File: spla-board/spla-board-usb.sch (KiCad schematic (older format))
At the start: 27 parts, among them J1 USB_B_Micro, U2 FT2232H, U3 93LC66B, X1 FT5HNBPK12.0-T1

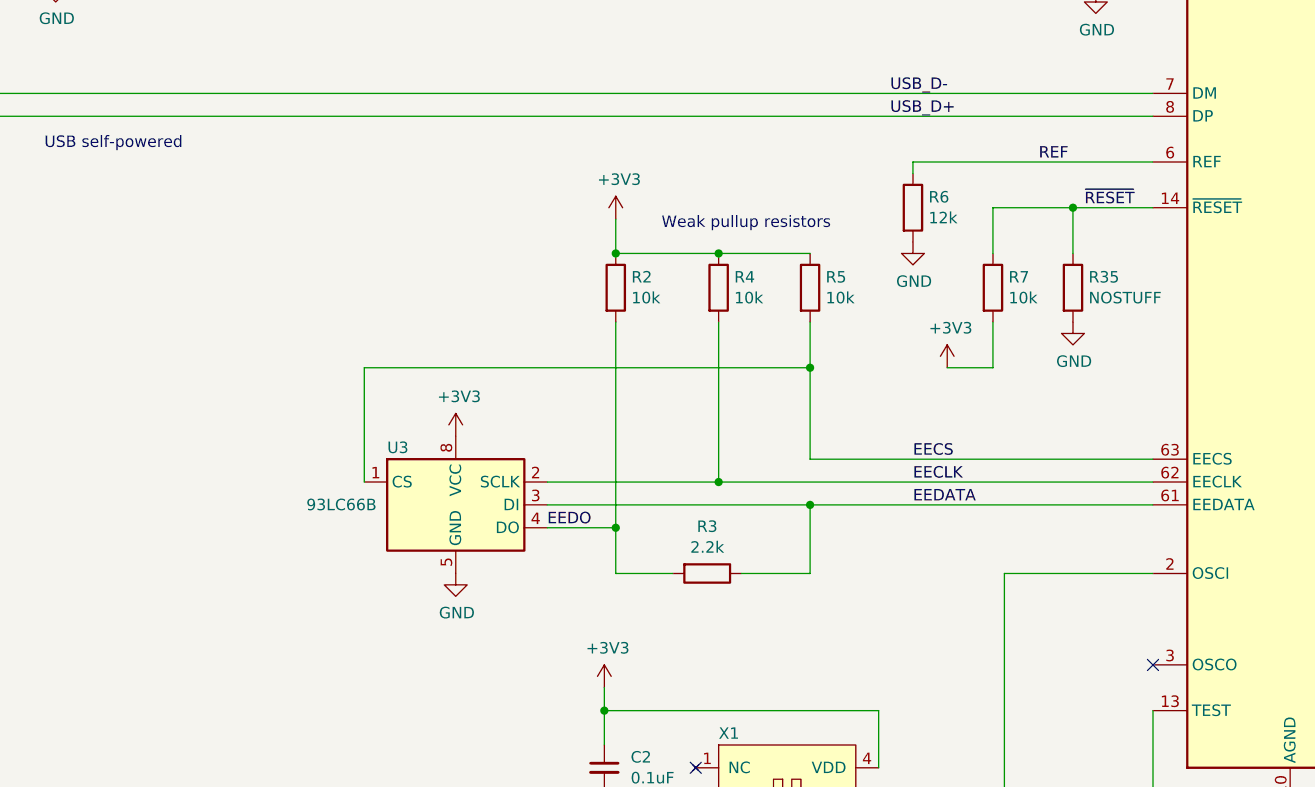
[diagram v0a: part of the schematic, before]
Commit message: schematic: Swap FTDI REF resistor from 5% (oops) to 1%.
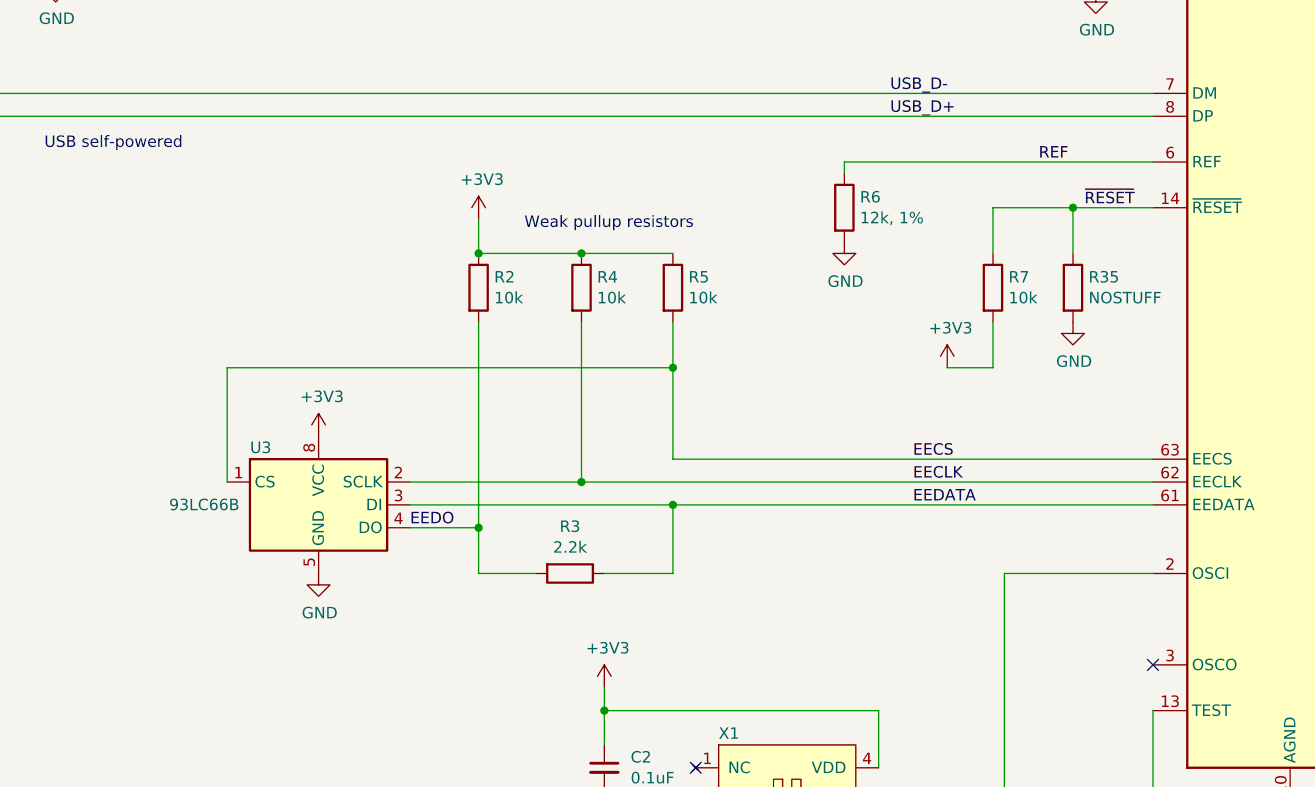
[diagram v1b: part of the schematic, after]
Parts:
- R6: value 12k -> 12k, 1%; Digikey RMCF0603JT12K0CT-ND -> RMCF0603FT12K0CT-ND; Manufacturer Id RMCF0603JT12K0 -> RMCF0603FT12K0
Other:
- moved on the sheet: R2, R3, R4, R5, R6, U3
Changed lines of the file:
@@
 L power:GND #PWR0104
 U 1 1 5E558255
-P 5700 6850
-F 0 "#PWR0104" H 5700 6600 50  0001 C CNN
-F 1 "GND" H 5705 6677 50  0000 C CNN
-F 2 "" H 5700 6850 50  0001 C CNN
-F 3 "" H 5700 6850 50  0001 C CNN
-	1    5700 6850
-	1    0    0    -1
-$EndComp
-Wire Wire Line
-	7250 6350 8750 6350
-Wire Wire Line
-	5300 5950 7250 5950
-Wire Wire Line
-	5300 5950 5300 6450
-Wire Wire Line
-	7250 5950 7250 6350
+P 5100 6850
+F 0 "#PWR0104" H 5100 6600 50  0001 C CNN
+F 1 "GND" H 5105 6677 50  0000 C CNN
+F 2 "" H 5100 6850 50  0001 C CNN
+F 3 "" H 5100 6850 50  0001 C CNN
+	1    5100 6850
+	1    0    0    -1
+$EndComp
+Wire Wire Line
+	6650 6350 8750 6350
+Wire Wire Line
+	4700 5950 6650 5950
+Wire Wire Line
+	4700 5950 4700 6450
+Wire Wire Line
+	6650 5950 6650 6350
 $Comp
 L Device:R R3
 U 1 1 5E55BD51
-P 6800 6850
-F 0 "R3" V 6595 6850 50  0000 C CNN
-F 1 "2.2k" V 6686 6850 50  0000 C CNN
-F 2 "Resistor_SMD:R_0603_1608Metric" V 6840 6840 50  0001 C CNN
-F 3 "~" H 6800 6850 50  0001 C CNN
-F 4 "RMCF0603JT2K20CT-ND" H 6800 6850 50  0001 C CNN "Digikey"
-F 5 "Stackpole Electronics Inc" H 6800 6850 50  0001 C CNN "Manufacturer"
-F 6 "RMCF0603JT2K20" H 6800 6850 50  0001 C CNN "Manufacturer Id"
-	1    6800 6850
+P 6200 6850
+F 0 "R3" V 5995 6850 50  0000 C CNN
+F 1 "2.2k" V 6086 6850 50  0000 C CNN
+F 2 "Resistor_SMD:R_0603_1608Metric" V 6240 6840 50  0001 C CNN
+F 3 "~" H 6200 6850 50  0001 C CNN
+F 4 "RMCF0603JT2K20CT-ND" H 6200 6850 50  0001 C CNN "Digikey"
+F 5 "Stackpole Electronics Inc" H 6200 6850 50  0001 C CNN "Manufacturer"
+F 6 "RMCF0603JT2K20" H 6200 6850 50  0001 C CNN "Manufacturer Id"
+	1    6200 6850
 	0    1    1    0
 $EndComp
 Wire Wire Line
-	6100 6650 6400 6650
-Wire Wire Line
-	6400 6650 6400 6850
-Wire Wire Line
-	6400 6850 6650 6850
-Wire Wire Line
-	6100 6550 7250 6550
-Wire Wire Line
-	6950 6850 7250 6850
-Wire Wire Line
-	6100 6450 6850 6450
-Wire Wire Line
-	7250 6550 7250 6850
-Wire Wire Line
-	8750 6550 7250 6550
-Connection ~ 7250 6550
-Wire Wire Line
-	7250 5450 6850 5450
-Connection ~ 6850 5450
-Wire Wire Line
-	6850 5450 6400 5450
-Wire Wire Line
-	6400 5450 6400 5300
-Connection ~ 6400 5450
-Wire Wire Line
-	6400 5750 6400 6650
-Connection ~ 6400 6650
-Wire Wire Line
-	6850 5750 6850 6450
-Connection ~ 6850 6450
-Wire Wire Line
-	6850 6450 8750 6450
-Wire Wire Line
-	7250 5750 7250 5950
-Connection ~ 7250 5950
+	5500 6650 5800 6650
+Wire Wire Line
+	5800 6650 5800 6850
+Wire Wire Line
+	5800 6850 6050 6850
+Wire Wire Line
+	5500 6550 6650 6550
+Wire Wire Line
+	6350 6850 6650 6850
+Wire Wire Line
+	5500 6450 6250 6450
+Wire Wire Line
+	6650 6550 6650 6850
+Wire Wire Line
+	8750 6550 6650 6550
+Connection ~ 6650 6550
+Wire Wire Line
+	6650 5450 6250 5450
+Connection ~ 6250 5450
+Wire Wire Line
+	6250 5450 5800 5450
+Wire Wire Line
+	5800 5450 5800 5300
+Connection ~ 5800 5450
+Wire Wire Line
+	5800 5750 5800 6650
+Connection ~ 5800 6650
+Wire Wire Line
+	6250 5750 6250 6450
+Connection ~ 6250 6450
+Wire Wire Line
+	6250 6450 8750 6450
+Wire Wire Line
+	6650 5750 6650 5950
+Connection ~ 6650 5950
 $Comp
 L power:GND #PWR0105
@@
 	8750 7850 8900 7850
 Connection ~ 8900 7850
-Text Notes 6600 5350 0    50   ~ 0
+Text Notes 6000 5350 0    50   ~ 0
 Weak pullup resistors
 Wire Wire Line
@@
 L power:GND #PWR0108
 U 1 1 5E616CF7
-P 7700 5400
-F 0 "#PWR0108" H 7700 5150 50  0001 C CNN
-F 1 "GND" H 7705 5227 50  0000 C CNN
-F 2 "" H 7700 5400 50  0001 C CNN
-F 3 "" H 7700 5400 50  0001 C CNN
-	1    7700 5400
-	1    0    0    -1
-$EndComp
-Wire Wire Line
-	7700 5050 7700 5100
+P 7400 5400
+F 0 "#PWR0108" H 7400 5150 50  0001 C CNN
+F 1 "GND" H 7405 5227 50  0000 C CNN
+F 2 "" H 7400 5400 50  0001 C CNN
+F 3 "" H 7400 5400 50  0001 C CNN
+	1    7400 5400
+	1    0    0    -1
+$EndComp
+Wire Wire Line
+	7400 5050 7400 5100
 Wire Wire Line
 	8050 5950 8050 5750
@@
 L power:+3V3 #PWR0110
 U 1 1 5E64A1B5
-P 5700 6250
-F 0 "#PWR0110" H 5700 6100 50  0001 C CNN
-F 1 "+3V3" H 5715 6423 50  0000 C CNN
-F 2 "" H 5700 6250 50  0001 C CNN
-F 3 "" H 5700 6250 50  0001 C CNN
-	1    5700 6250
+P 5100 6250
+F 0 "#PWR0110" H 5100 6100 50  0001 C CNN
+F 1 "+3V3" H 5115 6423 50  0000 C CNN
+F 2 "" H 5100 6250 50  0001 C CNN
+F 3 "" H 5100 6250 50  0001 C CNN
+	1    5100 6250
 	1    0    0    -1
 $EndComp
@@
 L power:+3V3 #PWR0112
 U 1 1 5E64B6A0
-P 6400 5300
-F 0 "#PWR0112" H 6400 5150 50  0001 C CNN
-F 1 "+3V3" H 6415 5473 50  0000 C CNN
-F 2 "" H 6400 5300 50  0001 C CNN
-F 3 "" H 6400 5300 50  0001 C CNN
-	1    6400 5300
+P 5800 5300
+F 0 "#PWR0112" H 5800 5150 50  0001 C CNN
+F 1 "+3V3" H 5815 5473 50  0000 C CNN
+F 2 "" H 5800 5300 50  0001 C CNN
+F 3 "" H 5800 5300 50  0001 C CNN
+	1    5800 5300
 	1    0    0    -1
 $EndComp
@@
 EECLK
 Wire Wire Line
-	7700 5050 8750 5050
+	7400 5050 8750 5050
 Text Label 8250 5050 0    50   ~ 0
 REF
@@
 Text Label 3450 4300 1    50   ~ 0
 USB_ID
-Text Label 6100 6650 0    50   ~ 0
+Text Label 5500 6650 0    50   ~ 0
 EEDO
 $Comp
@@
 L Memory_EEPROM:93LCxxB U3
 U 1 1 5E53A19A
-P 5700 6550
-F 0 "U3" H 5400 6800 50  0000 L CNN
-F 1 "93LC66B" H 5200 6550 50  0000 C CNN
-F 2 "Package_SO:SOIC-8_3.9x4.9mm_P1.27mm" H 5700 6550 50  0001 C CNN
-F 3 "http://ww1.microchip.com/downloads/en/DeviceDoc/20001749K.pdf" H 5700 6550 50  0001 C CNN
-F 4 "93LC66B/SN-ND" H 5700 6550 50  0001 C CNN "Digikey"
-F 5 "93LC66B/SN" H 5700 6550 50  0001 C CNN "Manufacturer Id"
-F 6 "Microchip Technology" H 5700 6550 50  0001 C CNN "Manufacturer"
-	1    5700 6550
+P 5100 6550
+F 0 "U3" H 4800 6800 50  0000 L CNN
+F 1 "93LC66B" H 4600 6550 50  0000 C CNN
+F 2 "Package_SO:SOIC-8_3.9x4.9mm_P1.27mm" H 5100 6550 50  0001 C CNN
+F 3 "http://ww1.microchip.com/downloads/en/DeviceDoc/20001749K.pdf" H 5100 6550 50  0001 C CNN
+F 4 "93LC66B/SN-ND" H 5100 6550 50  0001 C CNN "Digikey"
+F 5 "93LC66B/SN" H 5100 6550 50  0001 C CNN "Manufacturer Id"
+F 6 "Microchip Technology" H 5100 6550 50  0001 C CNN "Manufacturer"
+	1    5100 6550
 	1    0    0    -1
 $EndComp
@@
 L Device:R R6
 U 1 1 5E60E8AF
-P 7700 5250
-F 0 "R6" H 7768 5296 50  0000 L CNN
-F 1 "12k" H 7768 5205 50  0000 L CNN
-F 2 "Resistor_SMD:R_0603_1608Metric" V 7740 5240 50  0001 C CNN
-F 3 "~" H 7700 5250 50  0001 C CNN
-F 4 "RMCF0603JT12K0CT-ND" H 7700 5250 50  0001 C CNN "Digikey"
-F 5 "Stackpole Electronics Inc" H 7700 5250 50  0001 C CNN "Manufacturer"
-F 6 "RMCF0603JT12K0" H 7700 5250 50  0001 C CNN "Manufacturer Id"
-	1    7700 5250
+P 7400 5250
+F 0 "R6" H 7468 5296 50  0000 L CNN
+F 1 "12k, 1%" H 7468 5205 50  0000 L CNN
+F 2 "Resistor_SMD:R_0603_1608Metric" V 7440 5240 50  0001 C CNN
+F 3 "~" H 7400 5250 50  0001 C CNN
+F 4 "RMCF0603FT12K0CT-ND" H 7400 5250 50  0001 C CNN "Digikey"
+F 5 "Stackpole Electronics Inc" H 7400 5250 50  0001 C CNN "Manufacturer"
+F 6 "RMCF0603FT12K0" H 7400 5250 50  0001 C CNN "Manufacturer Id"
+	1    7400 5250
 	1    0    0    -1
 $EndComp
@@
 L Device:R R5
 U 1 1 5E572B74
-P 7250 5600
-F 0 "R5" H 7318 5646 50  0000 L CNN
-F 1 "10k" H 7318 5555 50  0000 L CNN
-F 2 "Resistor_SMD:R_0603_1608Metric" V 7290 5590 50  0001 C CNN
-F 3 "~" H 7250 5600 50  0001 C CNN
-F 4 "RMCF0603JT10K0CT-ND" H 7250 5600 50  0001 C CNN "Digikey"
-F 5 "Stackpole Electronics Inc" H 7250 5600 50  0001 C CNN "Manufacturer"
-F 6 "RMCF0603JT10K0" H 7250 5600 50  0001 C CNN "Manufacturer Id"
-	1    7250 5600
+P 6650 5600
+F 0 "R5" H 6718 5646 50  0000 L CNN
+F 1 "10k" H 6718 5555 50  0000 L CNN
+F 2 "Resistor_SMD:R_0603_1608Metric" V 6690 5590 50  0001 C CNN
+F 3 "~" H 6650 5600 50  0001 C CNN
+F 4 "RMCF0603JT10K0CT-ND" H 6650 5600 50  0001 C CNN "Digikey"
+F 5 "Stackpole Electronics Inc" H 6650 5600 50  0001 C CNN "Manufacturer"
+F 6 "RMCF0603JT10K0" H 6650 5600 50  0001 C CNN "Manufacturer Id"
+	1    6650 5600
 	1    0    0    -1
 $EndComp
@@
 L Device:R R4
 U 1 1 5E572548
-P 6850 5600
-F 0 "R4" H 6918 5646 50  0000 L CNN
-F 1 "10k" H 6918 5555 50  0000 L CNN
-F 2 "Resistor_SMD:R_0603_1608Metric" V 6890 5590 50  0001 C CNN
-F 3 "~" H 6850 5600 50  0001 C CNN
-F 4 "RMCF0603JT10K0CT-ND" H 6850 5600 50  0001 C CNN "Digikey"
-F 5 "Stackpole Electronics Inc" H 6850 5600 50  0001 C CNN "Manufacturer"
-F 6 "RMCF0603JT10K0" H 6850 5600 50  0001 C CNN "Manufacturer Id"
-	1    6850 5600
+P 6250 5600
+F 0 "R4" H 6318 5646 50  0000 L CNN
+F 1 "10k" H 6318 5555 50  0000 L CNN
+F 2 "Resistor_SMD:R_0603_1608Metric" V 6290 5590 50  0001 C CNN
+F 3 "~" H 6250 5600 50  0001 C CNN
+F 4 "RMCF0603JT10K0CT-ND" H 6250 5600 50  0001 C CNN "Digikey"
+F 5 "Stackpole Electronics Inc" H 6250 5600 50  0001 C CNN "Manufacturer"
+F 6 "RMCF0603JT10K0" H 6250 5600 50  0001 C CNN "Manufacturer Id"
+	1    6250 5600
 	1    0    0    -1
 $EndComp
@@
 L Device:R R2
 U 1 1 5E571C78
-P 6400 5600
-F 0 "R2" H 6468 5646 50  0000 L CNN
-F 1 "10k" H 6468 5555 50  0000 L CNN
-F 2 "Resistor_SMD:R_0603_1608Metric" V 6440 5590 50  0001 C CNN
-F 3 "~" H 6400 5600 50  0001 C CNN
-F 4 "RMCF0603JT10K0CT-ND" H 6400 5600 50  0001 C CNN "Digikey"
-F 5 "Stackpole Electronics Inc" H 6400 5600 50  0001 C CNN "Manufacturer"
-F 6 "RMCF0603JT10K0" H 6400 5600 50  0001 C CNN "Manufacturer Id"
-	1    6400 5600
-	1    0    0    -1
-$EndComp
+P 5800 5600
+F 0 "R2" H 5868 5646 50  0000 L CNN
+F 1 "10k" H 5868 5555 50  0000 L CNN
+F 2 "Resistor_SMD:R_0603_1608Metric" V 5840 5590 50  0001 C CNN
+F 3 "~" H 5800 5600 50  0001 C CNN
+F 4 "RMCF0603JT10K0CT-ND" H 5800 5600 50  0001 C CNN "Digikey"
+F 5 "Stackpole Electronics Inc" H 5800 5600 50  0001 C CNN "Manufacturer"
+F 6 "RMCF0603JT10K0" H 5800 5600 50  0001 C CNN "Manufacturer Id"
+	1    5800 5600
+	1    0    0    -1
+$EndComp

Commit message: schematic/pcb: Remove unnecessary 0-ohm resistors; renumber all parts by value.
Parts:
- R3: renamed from R35; Digikey RMCF0603JT1K00CT-ND -> N/A; Manufacturer Stackpole Electronics Inc -> N/A; Manufacturer Id RMCF0603JT1K00 -> N/A
- renumbered C2 to C14, C44 to C2, C5 to C3, C6 to C4, C3 to C51, C4 to C52, C7 to C53, R32 to R2, R12 to R27, R3 to R4, R2 to R50, R4 to R51, R5 to R52, R7 to R53, R31 to R59, R39 to R73, R6 to R8
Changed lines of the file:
@@
 	6650 5950 6650 6350
 $Comp
-L Device:R R3
+L Device:R R4
 U 1 1 5E55BD51
 P 6200 6850
-F 0 "R3" V 5995 6850 50  0000 C CNN
+F 0 "R4" V 5995 6850 50  0000 C CNN
 F 1 "2.2k" V 6086 6850 50  0000 C CNN
 F 2 "Resistor_SMD:R_0603_1608Metric" V 6240 6840 50  0001 C CNN
@@
 $EndComp
 $Comp
-L Device:R_Small R12
+L Device:R_Small R27
 U 1 1 5EB172EB
 P 12400 7050
-F 0 "R12" H 12459 7096 50  0000 L CNN
+F 0 "R27" H 12459 7096 50  0000 L CNN
 F 1 "330" H 12459 7005 50  0000 L CNN
 F 2 "Resistor_SMD:R_0603_1608Metric" H 12400 7050 50  0001 C CNN
@@
 	11900 5850 12000 5850
 $Comp
-L Device:R_Small R31
+L Device:R_Small R59
 U 1 1 5EB42683
 P 11900 5600
-F 0 "R31" H 11959 5646 50  0000 L CNN
+F 0 "R59" H 11959 5646 50  0000 L CNN
 F 1 "10k" H 11959 5555 50  0000 L CNN
 F 2 "Resistor_SMD:R_0603_1608Metric" H 11900 5600 50  0001 C CNN
@@
 Connection ~ 2700 3950
 $Comp
-L Device:C C7
-U 1 1 5E5E774C
-P 8500 4150
-F 0 "C7" H 8615 4196 50  0000 L CNN
-F 1 "4.7uF" H 8615 4105 50  0000 L CNN
-F 2 "Capacitor_SMD:C_0603_1608Metric" H 8538 4000 50  0001 C CNN
-F 3 "~" H 8500 4150 50  0001 C CNN
-F 4 "490-7203-1-ND" H 8500 4150 50  0001 C CNN "Digikey"
-F 5 "Murata Electronics" H 8500 4150 50  0001 C CNN "Manufacturer"
-F 6 "GRM188R61E475KE11D" H 8500 4150 50  0001 C CNN "Manufacturer Id"
-	1    8500 4150
-	1    0    0    -1
-$EndComp
-$Comp
-L Device:C C5
+L Device:C C3
 U 1 1 5E6D502E
 P 7800 2250
-F 0 "C5" H 7915 2296 50  0000 L CNN
+F 0 "C3" H 7915 2296 50  0000 L CNN
 F 1 "0.1uF" H 7915 2205 50  0000 L CNN
 F 2 "Capacitor_SMD:C_0603_1608Metric" H 7838 2100 50  0001 C CNN
@@
 $EndComp
 $Comp
-L Device:C C6
+L Device:C C4
 U 1 1 5E6D5FB8
 P 7800 2900
-F 0 "C6" H 7915 2946 50  0000 L CNN
+F 0 "C4" H 7915 2946 50  0000 L CNN
 F 1 "0.1uF" H 7915 2855 50  0000 L CNN
 F 2 "Capacitor_SMD:C_0603_1608Metric" H 7838 2750 50  0001 C CNN
@@
 $EndComp
 $Comp
-L Device:C C3
+L Device:C C51
 U 1 1 5E6D1368
 P 7300 2250
-F 0 "C3" H 7415 2296 50  0000 L CNN
+F 0 "C51" H 7415 2296 50  0000 L CNN
 F 1 "4.7uF" H 7415 2205 50  0000 L CNN
 F 2 "Capacitor_SMD:C_0603_1608Metric" H 7338 2100 50  0001 C CNN
@@
 $EndComp
 $Comp
-L Device:C C4
+L Device:C C52
 U 1 1 5E6D59EB
 P 7300 2900
-F 0 "C4" H 7415 2946 50  0000 L CNN
+F 0 "C52" H 7415 2946 50  0000 L CNN
 F 1 "4.7uF" H 7415 2855 50  0000 L CNN
 F 2 "Capacitor_SMD:C_0603_1608Metric" H 7338 2750 50  0001 C CNN
@@
 $EndComp
 $Comp
-L Device:R R7
+L Device:R R53
 U 1 1 5E619C52
 P 8050 5600
-F 0 "R7" H 8118 5646 50  0000 L CNN
+F 0 "R53" H 8118 5646 50  0000 L CNN
 F 1 "10k" H 8118 5555 50  0000 L CNN
 F 2 "Resistor_SMD:R_0603_1608Metric" V 8090 5590 50  0001 C CNN
@@
 $EndComp
 $Comp
-L Device:C_Small C2
+L Device:C_Small C14
 U 1 1 5E53DEA7
 P 6350 7700
-F 0 "C2" H 6465 7746 50  0000 L CNN
+F 0 "C14" H 6465 7746 50  0000 L CNN
 F 1 "0.1uF" H 6465 7655 50  0000 L CNN
 F 2 "Capacitor_SMD:C_0603_1608Metric" H 6388 7550 50  0001 C CNN
@@
 $EndComp
 $Comp
-L Device:R R6
+L Device:R R8
 U 1 1 5E60E8AF
 P 7400 5250
-F 0 "R6" H 7468 5296 50  0000 L CNN
+F 0 "R8" H 7468 5296 50  0000 L CNN
 F 1 "12k, 1%" H 7468 5205 50  0000 L CNN
 F 2 "Resistor_SMD:R_0603_1608Metric" V 7440 5240 50  0001 C CNN
@@
 $EndComp
 $Comp
-L Device:R R5
+L Device:R R52
 U 1 1 5E572B74
 P 6650 5600
-F 0 "R5" H 6718 5646 50  0000 L CNN
+F 0 "R52" H 6718 5646 50  0000 L CNN
 F 1 "10k" H 6718 5555 50  0000 L CNN
 F 2 "Resistor_SMD:R_0603_1608Metric" V 6690 5590 50  0001 C CNN
@@
 $EndComp
 $Comp
-L Device:R R4
+L Device:R R51
 U 1 1 5E572548
 P 6250 5600
-F 0 "R4" H 6318 5646 50  0000 L CNN
+F 0 "R51" H 6318 5646 50  0000 L CNN
 F 1 "10k" H 6318 5555 50  0000 L CNN
 F 2 "Resistor_SMD:R_0603_1608Metric" V 6290 5590 50  0001 C CNN
@@
 $Comp
 L Device:R R2
-U 1 1 5E571C78
-P 5800 5600
-F 0 "R2" H 5868 5646 50  0000 L CNN
-F 1 "10k" H 5868 5555 50  0000 L CNN
-F 2 "Resistor_SMD:R_0603_1608Metric" V 5840 5590 50  0001 C CNN
-F 3 "~" H 5800 5600 50  0001 C CNN
-F 4 "RMCF0603JT10K0CT-ND" H 5800 5600 50  0001 C CNN "Digikey"
-F 5 "Stackpole Electronics Inc" H 5800 5600 50  0001 C CNN "Manufacturer"
-F 6 "RMCF0603JT10K0" H 5800 5600 50  0001 C CNN "Manufacturer Id"
-	1    5800 5600
-	1    0    0    -1
-$EndComp
-$Comp
-L Device:R R32
 U 1 1 5F34ED5D
 P 2950 3550
-F 0 "R32" V 2750 3550 50  0000 C CNN
+F 0 "R2" V 2750 3550 50  0000 C CNN
 F 1 "NOSTUFF" V 2850 3550 50  0000 C CNN
 F 2 "Resistor_SMD:R_0603_1608Metric" H 2950 3550 50  0001 C CNN
@@
 	2700 3950 2800 3950
 $Comp
-L Device:C C44
+L Device:C C2
 U 1 1 5F34D947
 P 2950 3950
-F 0 "C44" V 2700 3950 50  0000 C CNN
+F 0 "C2" V 2700 3950 50  0000 C CNN
 F 1 "NOSTUFF" V 2800 3950 50  0000 C CNN
 F 2 "Capacitor_SMD:C_0603_1608Metric" H 2950 3950 50  0001 C CNN
@@
 	7550 7900 8100 7900
 $Comp
-L Device:R R35
+L Device:R R3
 U 1 1 5F34C3CC
 P 8400 5600
-F 0 "R35" H 8468 5646 50  0000 L CNN
+F 0 "R3" H 8468 5646 50  0000 L CNN
 F 1 "NOSTUFF" H 8468 5555 50  0000 L CNN
 F 2 "Resistor_SMD:R_0603_1608Metric" V 8440 5590 50  0001 C CNN
 F 3 "~" H 8400 5600 50  0001 C CNN
-F 4 "RMCF0603JT1K00CT-ND" H 8400 5600 50  0001 C CNN "Digikey"
-F 5 "Stackpole Electronics Inc" H 8400 5600 50  0001 C CNN "Manufacturer"
-F 6 "RMCF0603JT1K00" H 8400 5600 50  0001 C CNN "Manufacturer Id"
+F 4 "N/A" H 8400 5600 50  0001 C CNN "Digikey"
+F 5 "N/A" H 8400 5600 50  0001 C CNN "Manufacturer"
+F 6 "N/A" H 8400 5600 50  0001 C CNN "Manufacturer Id"
 	1    8400 5600
 	1    0    0    -1
@@
 	11900 5250 11900 5500
 $Comp
-L Device:R R39
+L Device:R R73
 U 1 1 5F36220C
 P 8500 3600
-F 0 "R39" H 8570 3646 50  0000 L CNN
+F 0 "R73" H 8570 3646 50  0000 L CNN
 F 1 "0" H 8570 3555 50  0000 L CNN
 F 2 "Resistor_SMD:R_0603_1608Metric" V 8430 3600 50  0001 C CNN
@@
 	10450 2900 10450 3000
 Connection ~ 10450 3000
+$Comp
+L Device:C C53
+U 1 1 5E5E774C
+P 8500 4150
+F 0 "C53" H 8615 4196 50  0000 L CNN
+F 1 "4.7uF" H 8615 4105 50  0000 L CNN
+F 2 "Capacitor_SMD:C_0603_1608Metric" H 8538 4000 50  0001 C CNN
+F 3 "~" H 8500 4150 50  0001 C CNN
+F 4 "490-7203-1-ND" H 8500 4150 50  0001 C CNN "Digikey"
+F 5 "Murata Electronics" H 8500 4150 50  0001 C CNN "Manufacturer"
+F 6 "GRM188R61E475KE11D" H 8500 4150 50  0001 C CNN "Manufacturer Id"
+	1    8500 4150
+	1    0    0    -1
+$EndComp
+$Comp
+L Device:R R50
+U 1 1 5E571C78
+P 5800 5600
+F 0 "R50" H 5868 5646 50  0000 L CNN
+F 1 "10k" H 5868 5555 50  0000 L CNN
+F 2 "Resistor_SMD:R_0603_1608Metric" V 5840 5590 50  0001 C CNN
+F 3 "~" H 5800 5600 50  0001 C CNN
+F 4 "RMCF0603JT10K0CT-ND" H 5800 5600 50  0001 C CNN "Digikey"
+F 5 "Stackpole Electronics Inc" H 5800 5600 50  0001 C CNN "Manufacturer"
+F 6 "RMCF0603JT10K0" H 5800 5600 50  0001 C CNN "Manufacturer Id"
+	1    5800 5600
+	1    0    0    -1
+$EndComp
 $EndSCHEMATC
